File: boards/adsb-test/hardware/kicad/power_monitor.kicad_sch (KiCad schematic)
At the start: 10 parts, among them U501 PAC1954 (PM1), U502 PAC1954 (PM2), U503 PAC1954 (PM3)

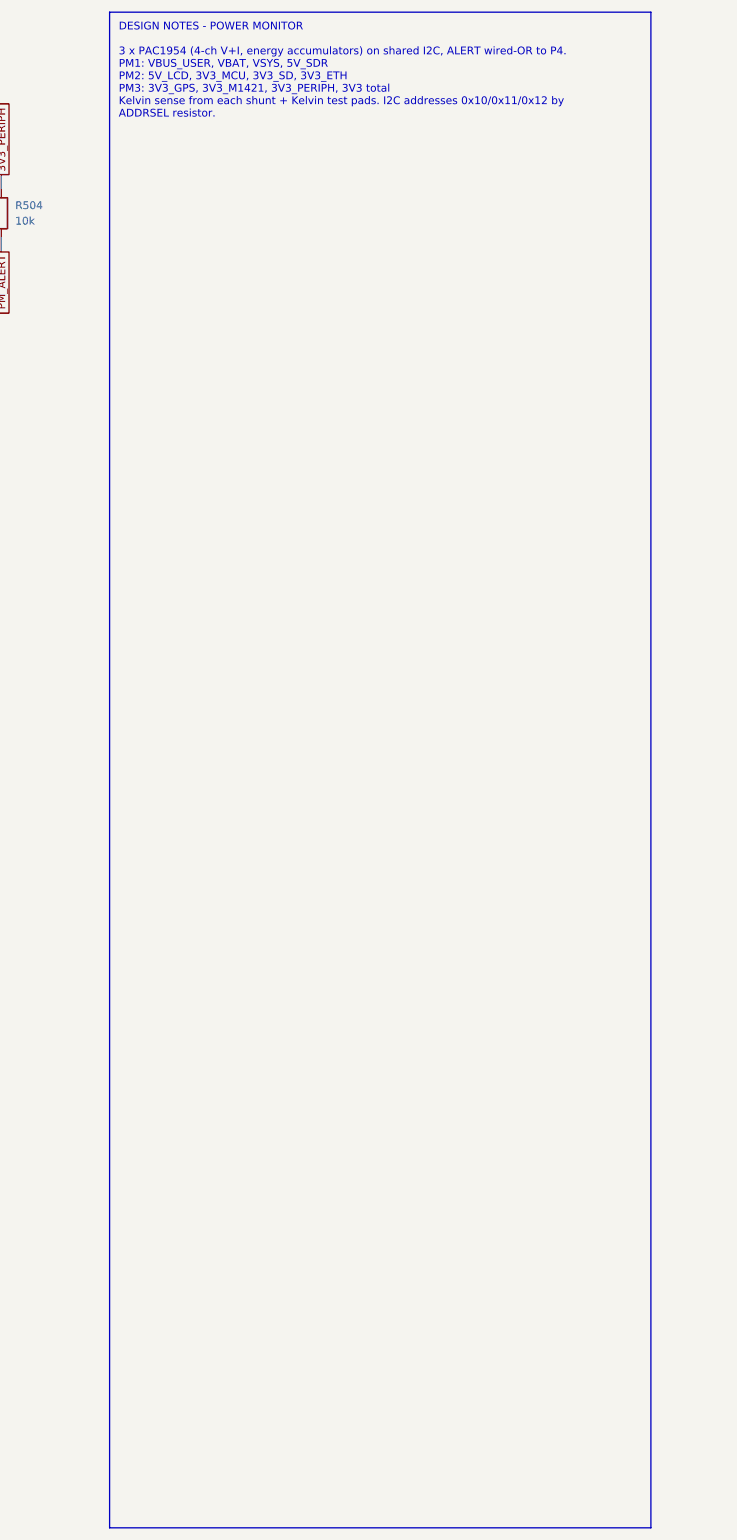
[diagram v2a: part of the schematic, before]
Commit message: ADSB_Test: Dev port split over three A3 sheets; old note boxes replaced with short current notes
Co-Authored-By: Claude Opus 5.5 <noreply@anthropic.com>
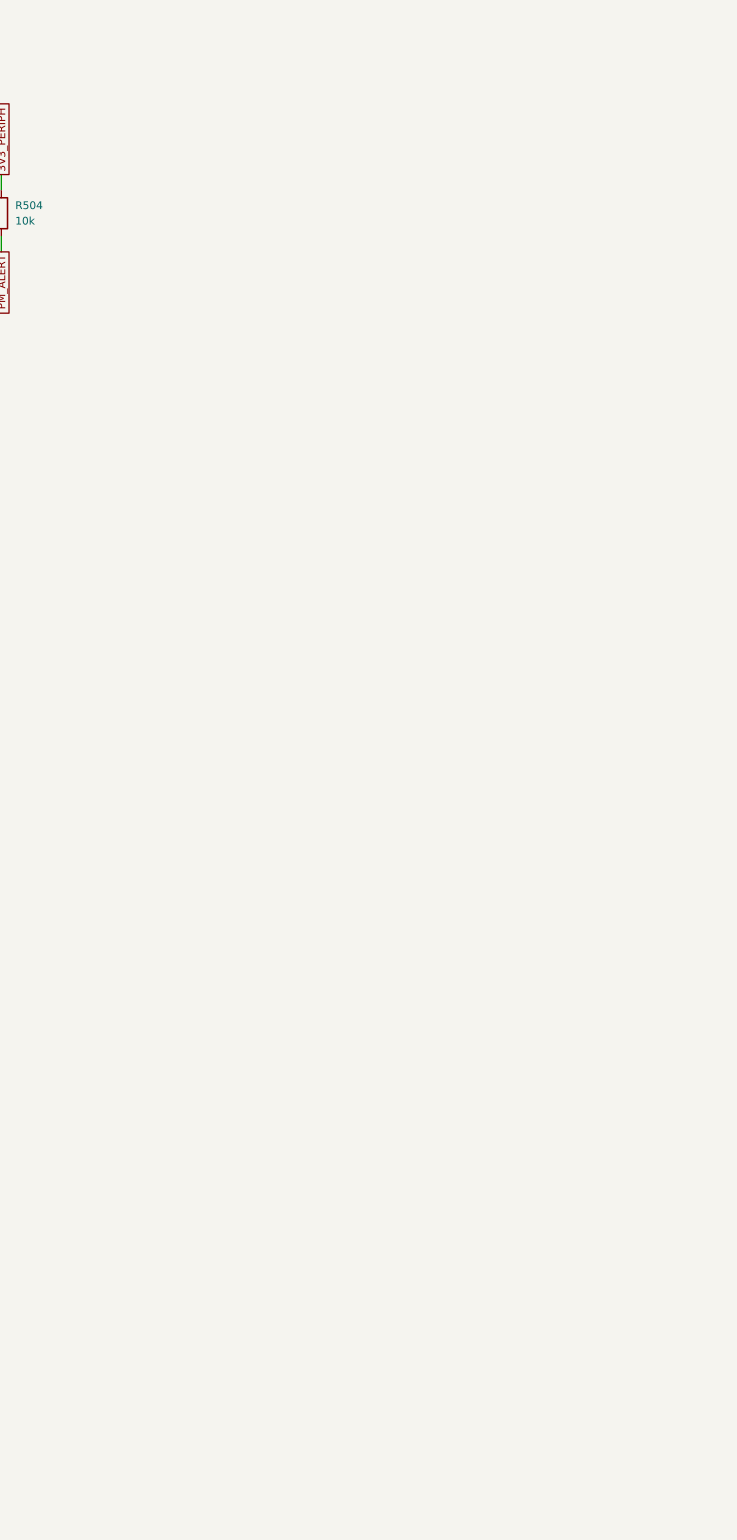
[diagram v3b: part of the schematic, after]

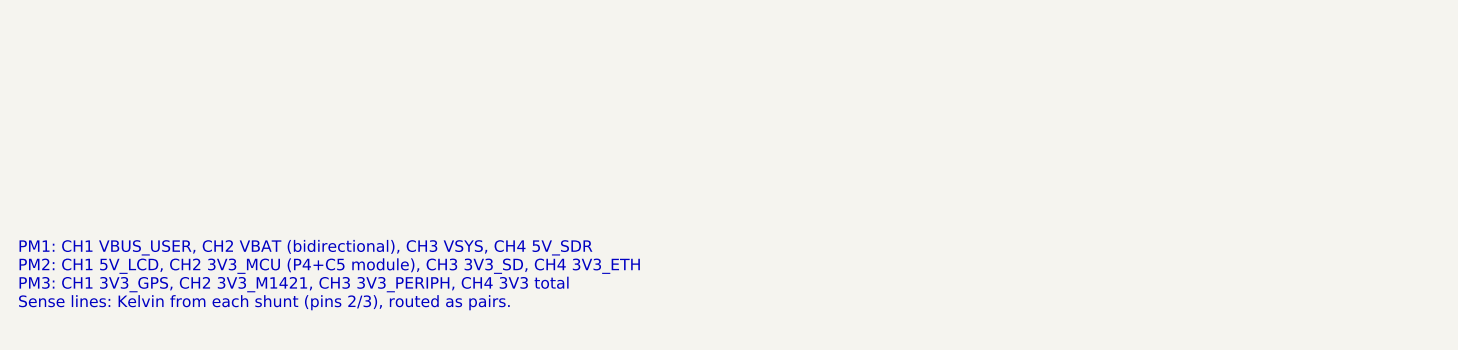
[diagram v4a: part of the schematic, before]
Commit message: ADSB_Test: current shunts resized for the PAC1954 100 mV range
Each shunt now gives ~40-75 mV at its rail's expected peak (several light
rails gave 2-20 mV): battery/VSYS 20m, 3V3 total 30m, 5V_SDR 50m, 3V3_SD
330m, 3V3_ETH 1R, m1421 and 3V3_PERIPH 2.2R. Full-scale currents on the
Power Monitor sheet, BOM updated, PCB regenerated (user's KiCad moves
captured into PLACE first; nothing moved, parity 0).

Co-Authored-By: Claude Opus 5.5 <noreply@anthropic.com>
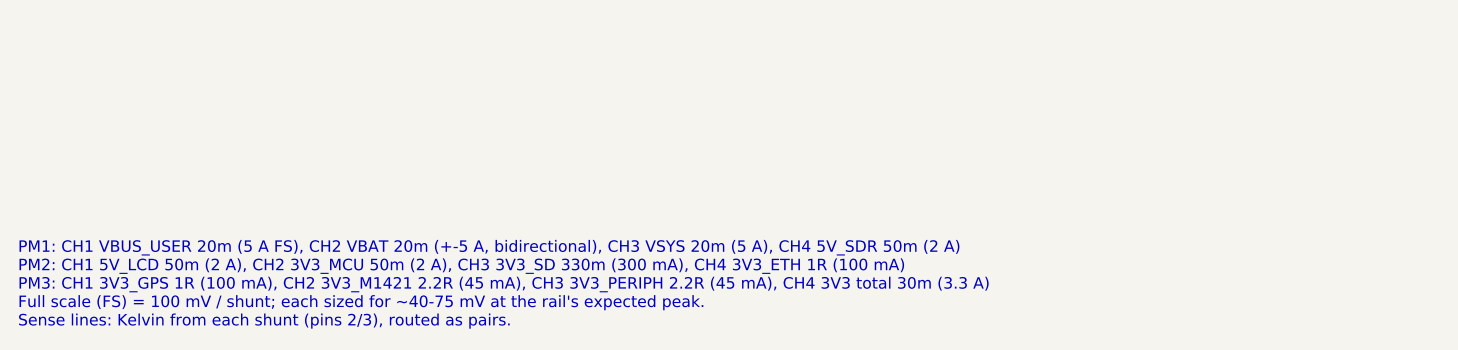
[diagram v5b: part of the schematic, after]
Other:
- note added: "PM1: CH1 VBUS_USER 20m (5 A FS), CH2 VBAT 20m (+-5 A, bidirectional), CH3 VSYS 20m (5 A), CH4 5V_SDR 50m (2 A) PM2: CH1 5V_LCD 50m (2 A), CH2 3V3_MCU 50m (2 A), CH3 3V3_SD 330m (300 mA), CH4 3V3_ETH 1R (100 mA) PM3: CH1 3V3_GPS 1R (100 mA), CH2 3V3_M1421 2.2R (45 mA), CH3 3V3_PERIPH 2.2R (45 mA), CH4 3V3 total 30m (3.3 A) Full scale (FS) = 100 mV / shunt; each sized for ~40-75 mV at the rail's ex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"
- note removed: "PM1: CH1 VBUS_USER, CH2 VBAT (bidirectional), CH3 VSYS, CH4 5V_SDR PM2: CH1 5V_LCD, CH2 3V3_MCU (P4+C5 module), CH3 3V3_SD, CH4 3V3_ETH PM3: CH1 3V3_GPS, CH2 3V3_M1421, CH3 3V3_PERIPH, CH4 3V3 total Sense lines: Kelvin from each shunt (pins 2/3), routed as pairs."
